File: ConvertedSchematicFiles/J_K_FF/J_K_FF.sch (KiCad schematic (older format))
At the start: 14 parts, among them U1 7476, U2 7476

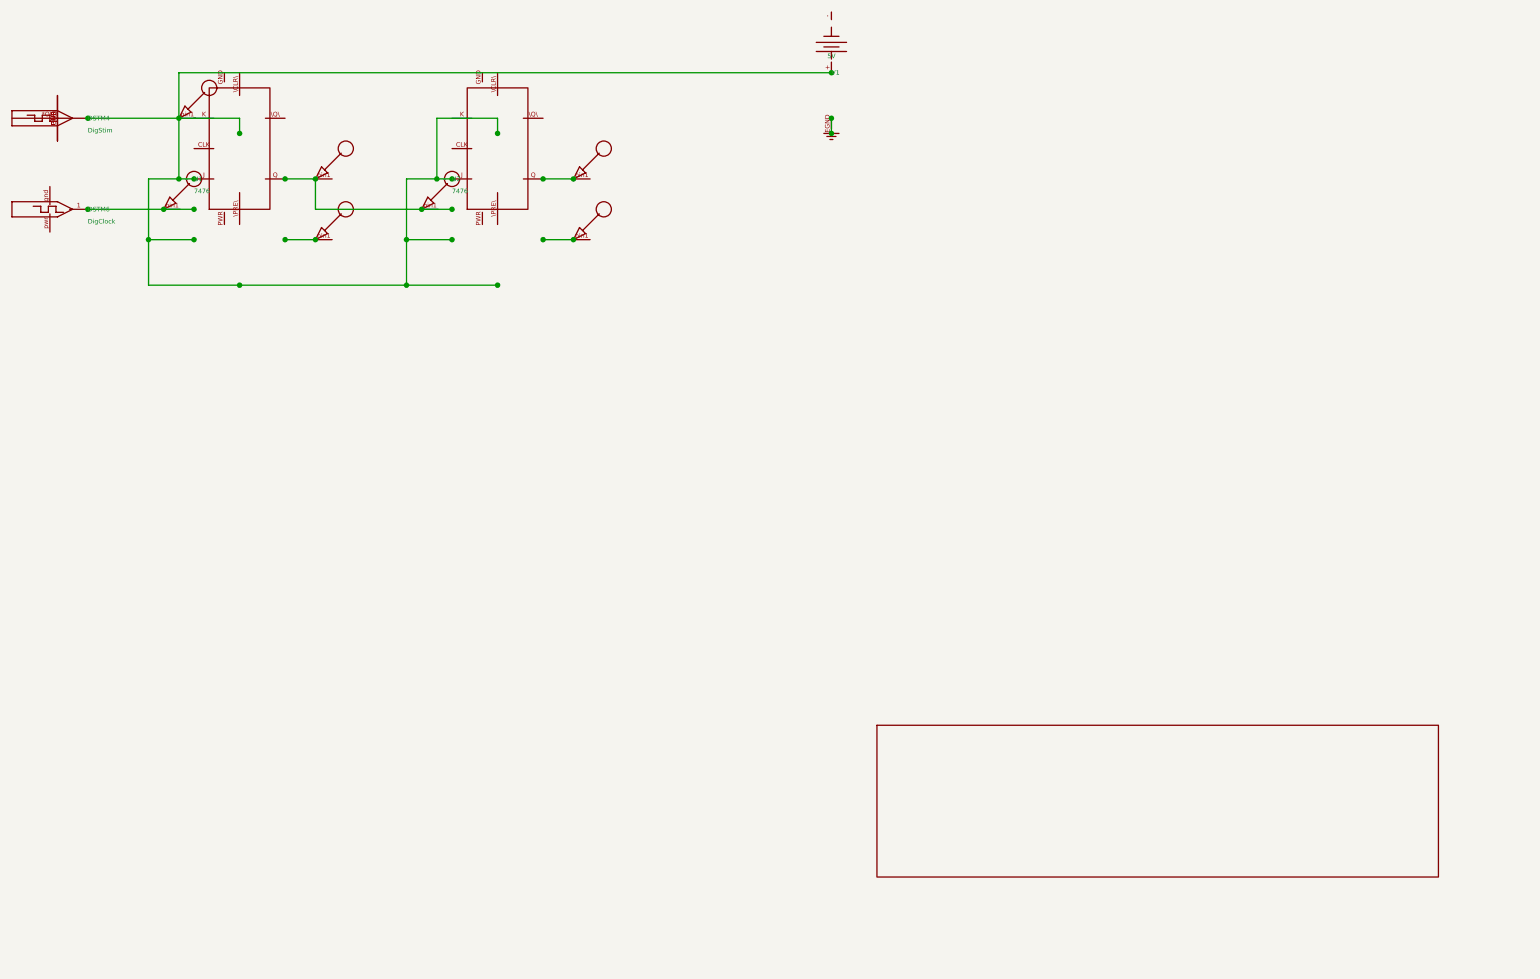
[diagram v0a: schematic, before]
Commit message: Excluded some components. These no longer appear after conversion. When calling shell commands, filenames are in "quotes"
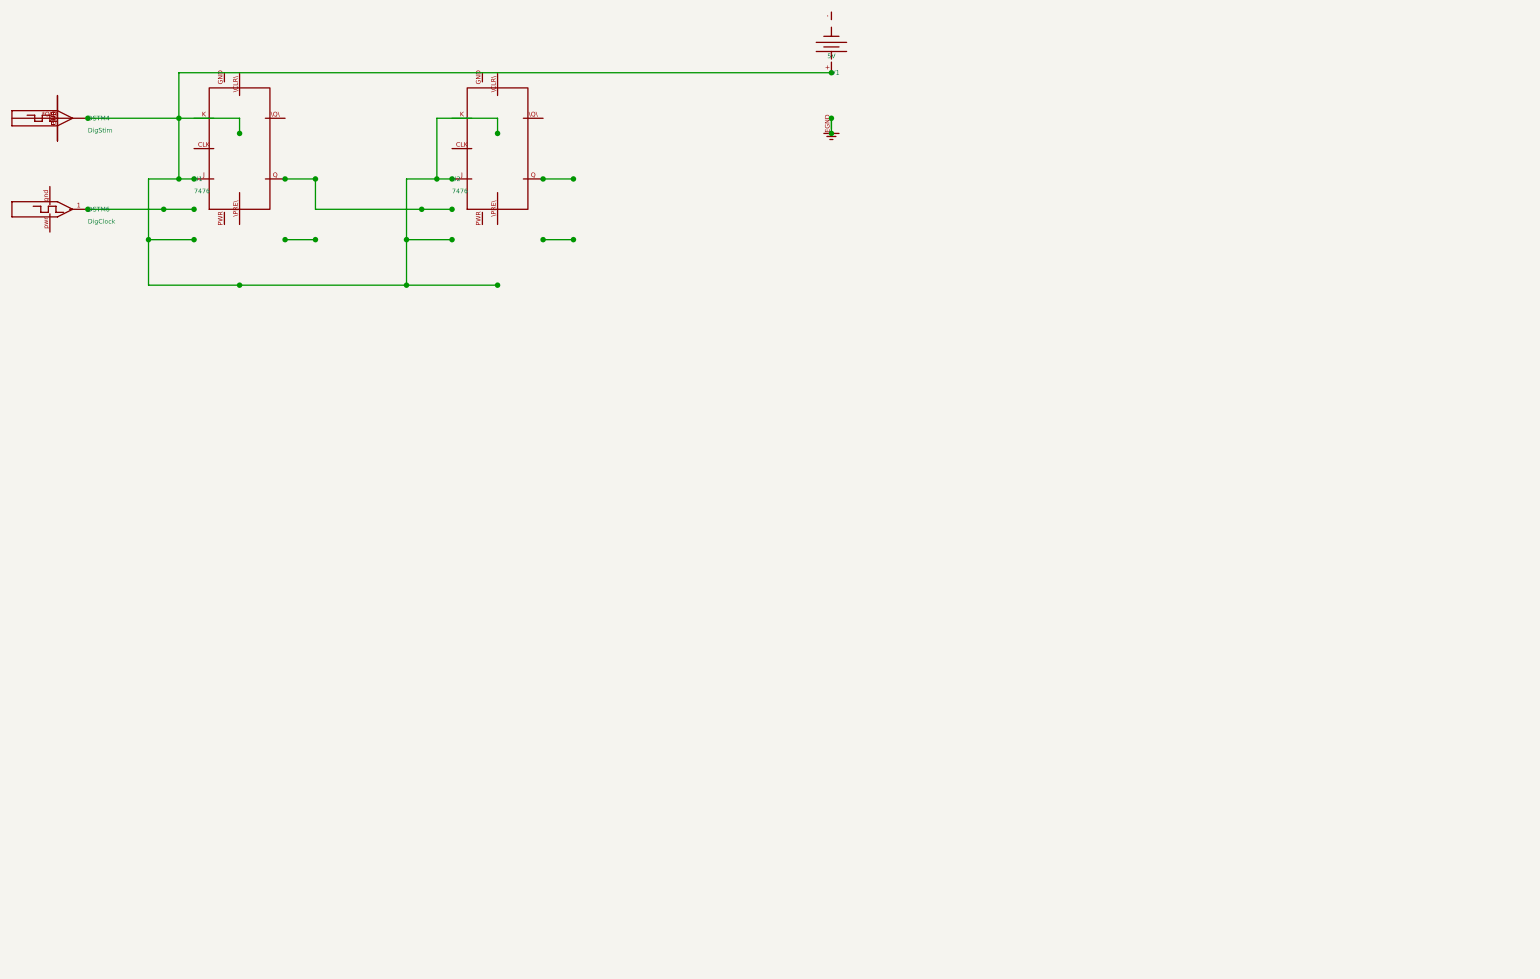
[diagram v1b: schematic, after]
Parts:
- removed nodeMarker (x7): nodeMarker, symbol NODEMARKER_PSPICE
- removed titleblk: titleblk, symbol TITLEBLK_PSPICE
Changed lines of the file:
@@
-	1    0    0    1
-$EndComp
-$Comp
-L TITLEBLK_PSPICE titleblk
-U 1 1 99885386
-P 9700 7200
-F 0 "titleblk" H 19400 14400 30  0001 L CNN
-F 1 "titleblk" H 19400 14480 30  0001 L CNN
-	1    9700 7200
-	1    0    0    1
-$EndComp
-$Comp
-L NODEMARKER_PSPICE nodeMarker
-U 1 1 39760492
-P 1300 2800
-F 0 "nodeMarker" H 2600 5600 30  0001 L CNN
-F 1 "nodeMarker" H 2600 5680 30  0001 L CNN
-	1    1300 2800
-	1    0    0    1
-$EndComp
-$Comp
-L NODEMARKER_PSPICE nodeMarker
-U 1 1 66516649
-P 2300 3000
-F 0 "nodeMarker" H 4600 6000 30  0001 L CNN
-F 1 "nodeMarker" H 4600 6080 30  0001 L CNN
-	1    2300 3000
-	1    0    0    1
-$EndComp
-$Comp
-L NODEMARKER_PSPICE nodeMarker
-U 1 1 29641421
-P 4000 2600
-F 0 "nodeMarker" H 8000 5200 30  0001 L CNN
-F 1 "nodeMarker" H 8000 5280 30  0001 L CNN
-	1    4000 2600
-	1    0    0    1
-$EndComp
-$Comp
-L NODEMARKER_PSPICE nodeMarker
-U 1 1 45202362
-P 4000 3000
-F 0 "nodeMarker" H 8000 6000 30  0001 L CNN
-F 1 "nodeMarker" H 8000 6080 30  0001 L CNN
-	1    4000 3000
-	1    0    0    1
-$EndComp
-$Comp
-L NODEMARKER_PSPICE nodeMarker
-U 1 1 10490027
-P 3000 2800
-F 0 "nodeMarker" H 6000 5600 30  0001 L CNN
-F 1 "nodeMarker" H 6000 5680 30  0001 L CNN
-	1    3000 2800
-	1    0    0    1
-$EndComp
-$Comp
-L NODEMARKER_PSPICE nodeMarker
-U 1 1 73368690
-P 2300 2600
-F 0 "nodeMarker" H 4600 5200 30  0001 L CNN
-F 1 "nodeMarker" H 4600 5280 30  0001 L CNN
-	1    2300 2600
-	1    0    0    1
-$EndComp
-$Comp
-L NODEMARKER_PSPICE nodeMarker
-U 1 1 32520059
-P 1400 2200
-F 0 "nodeMarker" H 2800 4400 30  0001 L CNN
-F 1 "nodeMarker" H 2800 4480 30  0001 L CNN
-	1    1400 2200
 	1    0    0    1
 $EndComp

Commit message: Ports issue fixed. Now annotation for ports is #PWR? function added "itos"
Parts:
- removed EGND: EGND, symbol EGND_PSPICE
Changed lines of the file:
@@
 $EndDescr
 $Comp
-L EGND_PSPICE EGND
+L EGND_PSPICE #PWR1
 U 1 1 14289383
 P 5700 2200
-F 0 "EGND" H 11400 4400 30  0001 L CNN
+F 0 "#PWR1" H 11400 4400 30  0001 L CNN
 F 1 "EGND" H 11400 4480 30  0001 L CNN
 	1    5700 2200

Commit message: Added LICENSE.txt
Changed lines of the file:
@@
 $EndDescr
 $Comp
-L EGND_PSPICE #PWR1
+L GND #PWR1
 U 1 1 14289383
 P 5700 2200

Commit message: Orientation fix. Library components are now inverted, with +ve y axis going up. In Schematic files, +ve y axis is downwards. This is how the KiCad libraries are. As a result of the above fixed, the converted GND is now oriented correctly.
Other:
- moved on the sheet: U1, U2, V1
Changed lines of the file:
@@
 F 1 "EGND" H 11400 4480 30  0001 L CNN
 	1    5700 2200
-	1    0    0    1
+	1    0    0    -1
 $EndComp
 $Comp
@@
 F 1 "DigClock" H 800 2880 30  0000 L CNN
 	1    800 2800
-	1    0    0    1
+	1    0    0    -1
 $EndComp
 $Comp
@@
 F 1 "5V" H 5700 1790 30  0000 C CNN
 	1    5700 1900
-	1    0    0    1
+	1    0    0    -1
 $EndComp
 $Comp
@@
 F 1 "DigStim" H 800 2280 30  0000 L CNN
 	1    800 2200
-	1    0    0    1
+	1    0    0    -1
 $EndComp
 $Comp
@@
 F 1 "7476" H 1500 2680 30  0000 L CNN
 	1    1500 2600
-	1    0    0    1
+	1    0    0    -1
 $EndComp
 $Comp
@@
 F 1 "7476" H 3200 2680 30  0000 L CNN
 	1    3200 2600
-	1    0    0    1
+	1    0    0    -1
 $EndComp
 Wire Wire Line

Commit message: Removed the use of exec, wrote basename function, made integration with eSim easier.
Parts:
- added nodeMarker (x7): nodeMarker, symbol nodeMarker_PSPICE
- added titleblk: titleblk, symbol titleblk_PSPICE
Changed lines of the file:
@@
-EESchema Schematic File Version 2  date Saturday 17 July 1999 12:12:38 PM IST
+EESchema Schematic File Version 2  date
 LIBS:power
 LIBS:device
@@
 LIBS:contrib
 LIBS:valves
-LIBS:ConvertedSchematicFiles/J_K_FF-cache
 EELAYER 25  0
 EELAYER END
@@
 Sheet 1 1
 Title ""
-Date "17 Jul 1999"
+Date ""
 Rev ""
 Comp ""
@@
 	1    0    0    -1
 $EndComp
+$Comp
+L titleblk_PSPICE titleblk
+U 1 1 99885386
+P 9700 7200
+F 0 "titleblk" H 19400 14400 30  0001 L CNN
+F 1 "titleblk" H 19400 14480 30  0001 L CNN
+	1    9700 7200
+	1    0    0    -1
+$EndComp
+$Comp
+L nodeMarker_PSPICE nodeMarker
+U 1 1 39760492
+P 1300 2800
+F 0 "nodeMarker" H 2600 5600 30  0001 L CNN
+F 1 "nodeMarker" H 2600 5680 30  0001 L CNN
+	1    1300 2800
+	1    0    0    -1
+$EndComp
+$Comp
+L nodeMarker_PSPICE nodeMarker
+U 1 1 66516649
+P 2300 3000
+F 0 "nodeMarker" H 4600 6000 30  0001 L CNN
+F 1 "nodeMarker" H 4600 6080 30  0001 L CNN
+	1    2300 3000
+	1    0    0    -1
+$EndComp
+$Comp
+L nodeMarker_PSPICE nodeMarker
+U 1 1 29641421
+P 4000 2600
+F 0 "nodeMarker" H 8000 5200 30  0001 L CNN
+F 1 "nodeMarker" H 8000 5280 30  0001 L CNN
+	1    4000 2600
+	1    0    0    -1
+$EndComp
+$Comp
+L nodeMarker_PSPICE nodeMarker
+U 1 1 45202362
+P 4000 3000
+F 0 "nodeMarker" H 8000 6000 30  0001 L CNN
+F 1 "nodeMarker" H 8000 6080 30  0001 L CNN
+	1    4000 3000
+	1    0    0    -1
+$EndComp
+$Comp
+L nodeMarker_PSPICE nodeMarker
+U 1 1 10490027
+P 3000 2800
+F 0 "nodeMarker" H 6000 5600 30  0001 L CNN
+F 1 "nodeMarker" H 6000 5680 30  0001 L CNN
+	1    3000 2800
+	1    0    0    -1
+$EndComp
+$Comp
+L nodeMarker_PSPICE nodeMarker
+U 1 1 73368690
+P 2300 2600
+F 0 "nodeMarker" H 4600 5200 30  0001 L CNN
+F 1 "nodeMarker" H 4600 5280 30  0001 L CNN
+	1    2300 2600
+	1    0    0    -1
+$EndComp
+$Comp
+L nodeMarker_PSPICE nodeMarker
+U 1 1 32520059
+P 1400 2200
+F 0 "nodeMarker" H 2800 4400 30  0001 L CNN
+F 1 "nodeMarker" H 2800 4480 30  0001 L CNN
+	1    1400 2200
+	1    0    0    -1
+$EndComp
